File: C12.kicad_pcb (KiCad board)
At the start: 4 copper layers, 90.3 x 26.6 mm, 85 parts, among them IC1 BD63573NUV-E2, IC3 74HC595BQ,115, J1 Conn_01x06, J2 Slot Connector, J3 Conn_01x06, U1 74AHC1G08, U15 MCP9700AT-ETT, U3 INA181, U4 LM393, U5 MIC5235-3.3, U6 AVR64DA48, U8 OPA521, X1 ASE-24MHz

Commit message: Initial commit
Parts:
- IC3: footprint _Samac:74HC595BQ115 -> RTB:74HC595BQ115
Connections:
- net /RailcomRX/RX+ renamed /Railcom/RX+
- net /RailcomRX/RX- renamed /Railcom/RX-
- IC1 pad 11: GNDD -> (no net)

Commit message: Initial commit
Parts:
- moved HS1 15.0 mm to (130.9, 32.5)

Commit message: initial
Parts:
- added Q1: BC847BDW1, Package_TO_SOT_SMD:SOT-363_SC-70-6, F.Cu at (140.1, 45.7)
- added R10: 68k, Resistor_SMD:R_0603_1608Metric, F.Cu at (117.8, 42.5)
- added R11: 33k, Resistor_SMD:R_0603_1608Metric, F.Cu at (119.2, 42.5)
- added R12: 10k, Resistor_SMD:R_0603_1608Metric, F.Cu at (92.7, 42.4)
- added R18: 220k, Resistor_SMD:R_0603_1608Metric, F.Cu at (115.6, 29.4)
- added R2: 100k, Resistor_SMD:R_0603_1608Metric, F.Cu at (116.3, 42.5)
- added R21: 9.1k, Resistor_SMD:R_0603_1608Metric, F.Cu at (115.6, 27.9)
- added R26: 160, Inductor_SMD:L_1206_3216Metric, F.Cu at (136.1, 44.8)
- added R32: 160, Inductor_SMD:L_1206_3216Metric, F.Cu at (136.1, 47.2)
- added R33: 1k, Inductor_SMD:L_0603_1608Metric, F.Cu at (136.9, 42.9)
- added R34: 1k, Inductor_SMD:L_0603_1608Metric, F.Cu at (137.0, 41.4)
- R36: value 10k -> 22k
- moved HS1 15.3 mm to (133.7, 17.5)
- moved R36 6.90 mm to (120.7, 42.5), turned to 90 degrees
- moved R35 4.17 mm to (141.0, 42.8)
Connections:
- IC1 pad 11: (no net) -> GNDD
- J2 pad 17: (no net) -> GNDD
- J2 pad 18: (no net) -> GNDD
- J2 pad 24: (no net) -> iCONFIG
- R36 pad 2: GNDD -> iLIM3
- U6 pad 16: (no net) -> iLIM0
- U6 pad 17: (no net) -> iLIM1
- U6 pad 18: (no net) -> iLIM2
- U6 pad 19: (no net) -> iLIM3
- U6 pad 20: (no net) -> iCONFIG
- U6 pad 22: (no net) -> iSENSE
- U6 pad 23: (no net) -> TRKgnd
- U6 pad 30: (no net) -> rSENSE
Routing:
- net TRKgnd: track 0.00 -> 53.6 mm
- net rSENSE: track 0.00 -> 50.3 mm, vias 0 -> 2
- net iLIM3: track 0.00 -> 38.2 mm
- net iLIM2: track 0.00 -> 36.4 mm
- net iLIM1: track 0.00 -> 34.8 mm
- net iLIM0: track 0.00 -> 33.2 mm
- net iCONFIG: track 0.00 -> 14.2 mm, vias 0 -> 2
- net Net-(R10-Pad1): track 6.26 -> 18.5 mm, vias 0 -> 2
- net Net-(Q1-Pad5): track 0.00 -> 7.06 mm
- net DCC-A': track 37.4 -> 44.3 mm, vias 2 -> 3
- net Net-(Q1-Pad2): track 0.00 -> 5.15 mm
- net iSENSE: track 59.6 -> 64.4 mm, vias 2 -> 3
- net V24.rx: track 16.7 -> 21.4 mm
- net ~V24.rts: track 22.4 -> 27.1 mm, vias 2 -> 0
- net GNDD: track 92.4 -> 87.7 mm, vias 51 -> 59
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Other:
- rule via_min_size: 0.6 -> 0.5
- board text added: "Debug"
- board text added: "fschum '24"
- board text removed: "F.Schumacher'22"

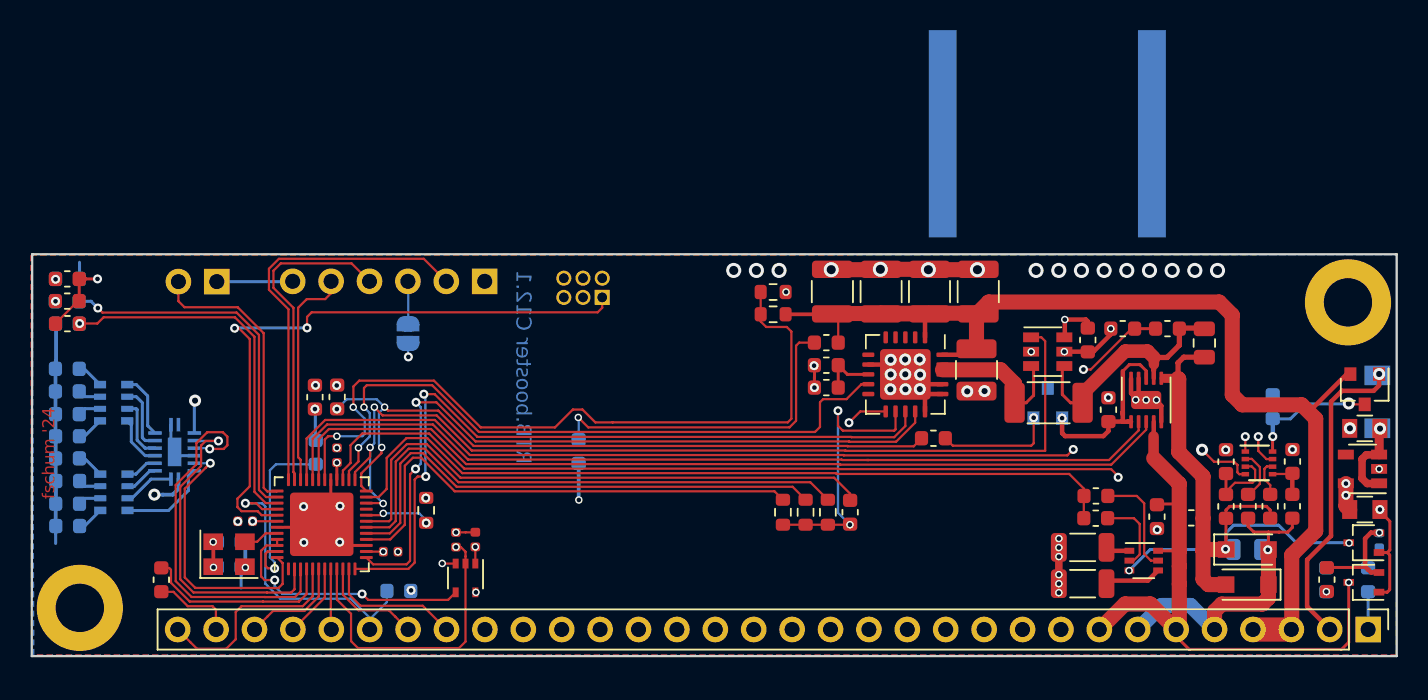
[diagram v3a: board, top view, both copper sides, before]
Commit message: mod: optimized for PCB assembly
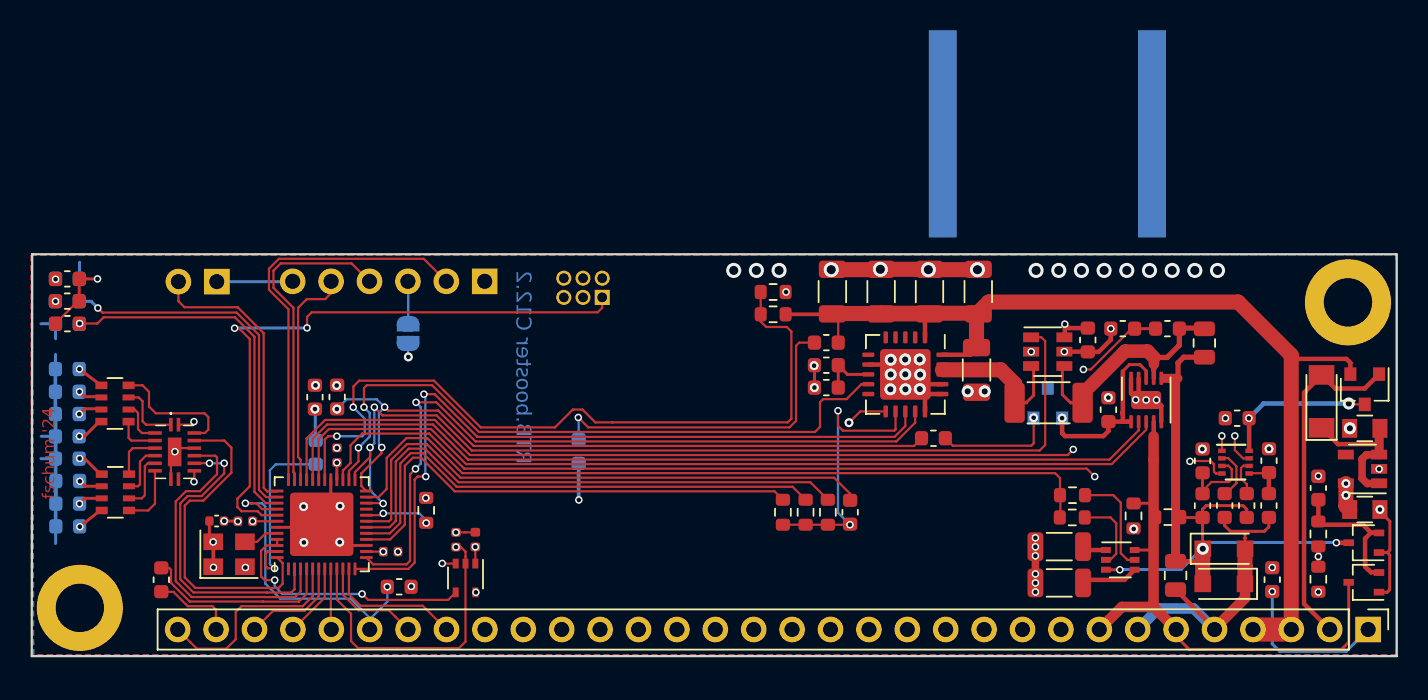
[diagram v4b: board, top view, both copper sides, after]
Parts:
- removed C7: 2.2u, Capacitor_SMD:C_0603_1608Metric
- C1: value 4.7uF -> 10uF; footprint Capacitor_SMD:C_1210_3225Metric -> Capacitor_SMD:C_1206_3216Metric
- C10, C14, C15, C20: value 100n -> 100nF
- C11: footprint Capacitor_SMD:C_0402_1005Metric -> Capacitor_SMD:C_0603_1608Metric; moved to F.Cu
- C19, C4, C8, C9: value 47uF -> 10uF; footprint Capacitor_SMD:C_1210_3225Metric -> Capacitor_SMD:C_1206_3216Metric
- C2: value 10uF/16V -> 10uF
- C3: value 2.2uF/10V -> 10uF
- C5: value 1u -> 1uF; moved to F.Cu
- C6: value 100n -> 100nF; footprint Capacitor_SMD:C_0603_1608Metric -> Capacitor_SMD:C_0402_1005Metric; moved to F.Cu
- D17, IC3, R14, R22, R29, R9: moved to F.Cu
- Q1: value BC847BDW1 -> BC847BDW1T1G
- R10: value 68k -> 56k
- R24: value 2.2k -> 3.3k
- R25: value 47k -> 3.3k
- R26, R32: value 160 -> 300
- R28, R39: value 100k -> 3.3k
- R30: value 6.8k -> 3.3k
- R33, R34, R35, R46: footprint Inductor_SMD:L_0603_1608Metric -> Resistor_SMD:R_0603_1608Metric
- R7, R8: value 80k -> 82k
- RN3, RN4: value 3.3k -> 4.7k; moved to F.Cu
- U3: value INA181 -> INA181A1
- U4: footprint _Local:DFN-8-1EP_NG_2x2mm_Pitch0.5mm -> RTB:DFN-8-1EP_NG_2x2mm_Pitch0.5mm
- moved D14 10.4 mm to (69.0, 43.4)
- moved D38 10.4 mm to (68.9, 33.0)
- moved D32 7.42 mm to (69.0, 41.9)
- moved D37 7.40 mm to (68.9, 34.5)
- moved R22 6.34 mm to (148.6, 47.0)
- moved RN4 5.93 mm to (72.1, 41.2)
- moved RN3 5.87 mm to (72.1, 35.3)
- moved C11 5.31 mm to (151.7, 40.9), turned to 90 degrees
- moved R9 5.05 mm to (142.2, 46.7), turned to 90 degrees
- moved D36 4.43 mm to (68.9, 36.0)
- moved D33 4.42 mm to (69.0, 40.4)
- moved D17 3.69 mm to (151.9, 35.2)
- moved R13 3.07 mm to (151.7, 43.9)
- moved C5 2.47 mm to (146.3, 36.3), turned to 0 degrees
- moved C6 1.61 mm to (78.8, 43.1)
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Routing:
- net Net-(J2-Pad1): track 2.50 -> 10.6 mm, vias 0 -> 1
- net Net-(C2-Pad1): track 7.00 -> 11.2 mm, vias 1 -> 0
- net MOSI0: track 18.1 -> 21.8 mm, vias 1 -> 0
- net SS0: track 25.4 -> 21.8 mm, vias 1 -> 0
- net VTRACK: track 6.66 -> 9.48 mm, vias 1 -> 0
- net Net-(IC3-Pad15): track 6.09 -> 8.56 mm
- net DCC-B: track 40.4 -> 38.1 mm, vias 1 -> 0
- net VREG: track 75.8 -> 73.6 mm
- net 3.3V: track 37.9 -> 36.0 mm
- net Vrail: track 20.8 -> 22.6 mm, vias 1 -> 0
- net Vrcm: track 8.66 -> 10.3 mm
- net Net-(R19-Pad2): track 61.5 -> 60.0 mm
- net RCM.pol: track 79.5 -> 78.0 mm
- net GNDD: track 87.7 -> 86.2 mm, vias 59 -> 65
- net DCC-A: track 20.4 -> 21.8 mm, vias 1 -> 0
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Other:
- rule pad_to_mask_clearance: 0.2 -> 0
- board text added: "RTB.booster C12.2"
- board text removed: "RTB.booster C12.1"

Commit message: mod: optimized for PCB assembly
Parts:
- C1, C19, C4, C8, C9: value 10uF -> 22uF
- J1: value Conn_01x06 -> Debug IF
- J3: value Conn_01x06 -> UPDI
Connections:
- net VTRACK renamed Net-(C11-Pad1)

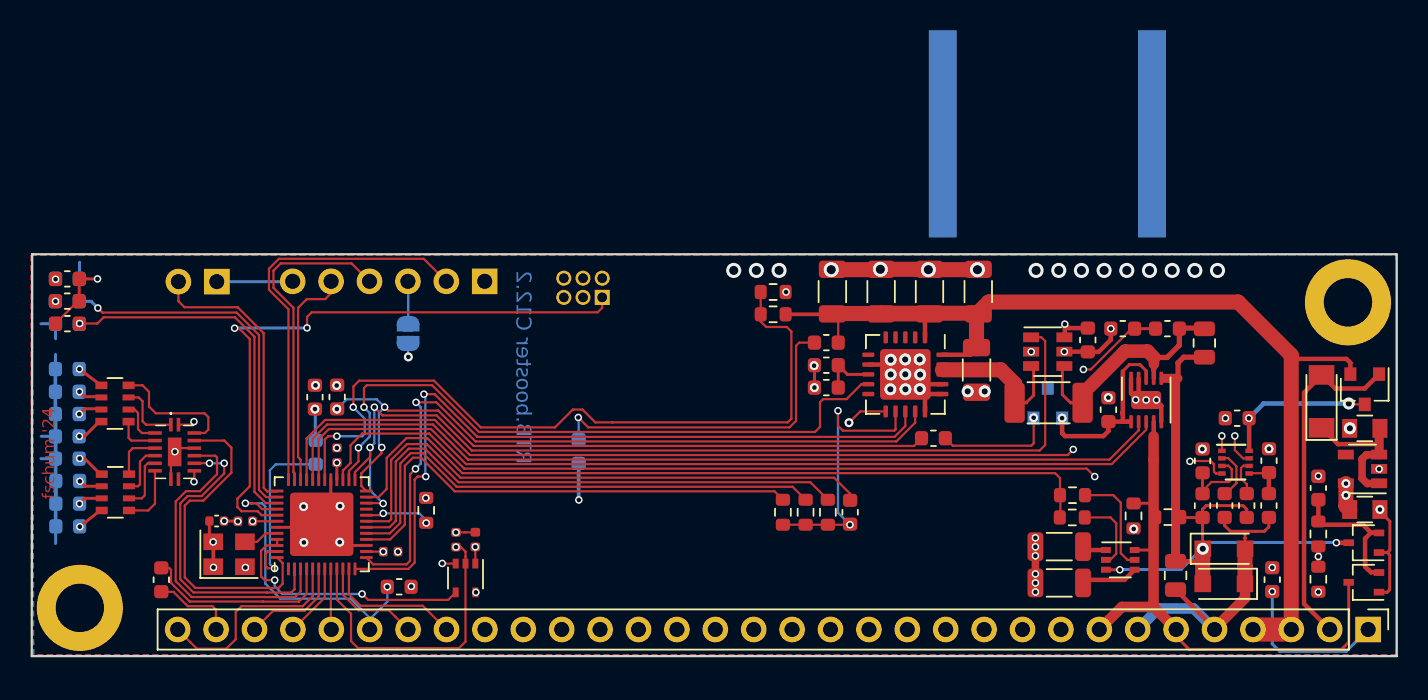
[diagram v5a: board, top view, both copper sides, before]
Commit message: upgrade to Kicad 9
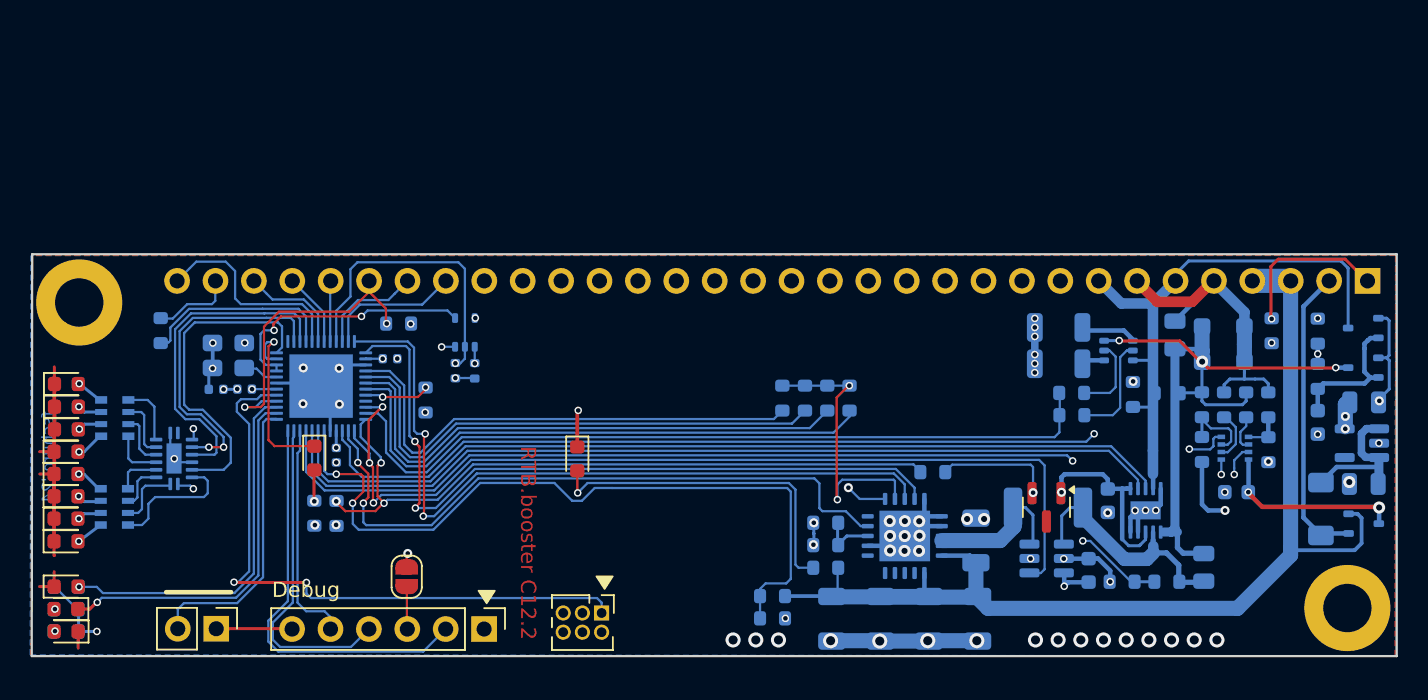
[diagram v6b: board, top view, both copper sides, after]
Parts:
- removed HS1: Heatsink, Heatsink:Heatsink_AAVID_573300D00010G_TO-263
- C1, C10, C11, C14, C15, C19, C20, C21, C4, C5, C6, C8, C9, D17, D3, D4, D6, D9, H1, H3, IC1, J2, R1, R10, R11, R12, R13, R14, R18, R19, R2, R20, R21, R22, R23, R24, R25, R26, R27, R28, R29, R3, R30, R31, R32, R33, R34, R35, R36, R37, R38, R39, R4, R46, R5, R6, R7, R8, R9, RN3, RN4, U1, U3, U4, U6, U8, X1: moved to B.Cu
- C2, C3: footprint Capacitors_SMD:C_0805 -> Capacitor_SMD:C_0805_2012Metric; moved to B.Cu
- D12, D13, D14, D16, D32, D33, D34, D35, D36, D37, D5, D8, J1, J3, JP1, JP2, U15: moved to F.Cu
- D31: footprint Package_TO_SOT_SMD:SOT-23 -> Package_TO_SOT_SMD:SOT-323_SC-70; moved to B.Cu
- D38: value LED_Small -> LED(wht); moved to F.Cu
- IC3: footprint RTB:74HC595BQ115 -> Package_DFN_QFN:DHVQFN-16-1EP_2.5x3.5mm_P0.5mm_EP1x2mm; moved to B.Cu
- Q1: value BC847BDW1T1G -> BC847BDW1; moved to B.Cu
- R15, R16: value 10k -> n.f.; moved to B.Cu
- R17: value 0.05 -> 0.025; moved to B.Cu
- U5: footprint TO_SOT_Packages_SMD:SOT-23-5 -> Package_TO_SOT_SMD:SOT-23-5; moved to B.Cu
- moved D16 23.3 mm to (68.8, 50.4)
- moved R28 23.3 mm to (68.8, 50.4)
- moved J2 23.1 mm to (154.9, 27.2), turned to 90 degrees
- moved J1 23.0 mm to (96.5, 50.2), turned to -90 degrees
- moved JP1 23.0 mm to (78.8, 50.2), turned to -90 degrees
- moved C19 21.6 mm to (122.7, 49.5), turned to -90 degrees
- moved C4 21.6 mm to (125.9, 49.5), turned to -90 degrees
- moved C8 21.6 mm to (129.1, 49.5), turned to -90 degrees
- moved C9 21.6 mm to (119.5, 49.5), turned to -90 degrees
- moved R21 21.6 mm to (115.6, 49.5)
- moved J3 20.9 mm to (104.3, 49.2), turned to -90 degrees
- moved R24 20.4 mm to (68.8, 48.9)
- moved D13 20.4 mm to (68.8, 48.9)
- moved H3 20.2 mm to (153.6, 48.8)
- moved H1 20.2 mm to (69.7, 28.6)
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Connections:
- net ~BUS.bsi renamed ~{BUS.bsi}
- net ~BUS.bso renamed ~{BUS.bso}
- net ~BUS.rts renamed ~{BUS.rts}
- net ~RESET renamed ~{RESET}
- net ~V24.cts renamed ~{V24.cts}
- net ~V24.rts renamed ~{V24.rts}
- IC3 pad 9: (no net) -> unconnected-(IC3-Q7S-Pad9)
- J2 pad 10: (no net) -> unconnected-(J2-Pin_10-Pad10)
- J2 pad 11: (no net) -> unconnected-(J2-Pin_11-Pad11)
- J2 pad 12: (no net) -> unconnected-(J2-Pin_12-Pad12)
- J2 pad 13: (no net) -> unconnected-(J2-Pin_13-Pad13)
- J2 pad 14: (no net) -> unconnected-(J2-Pin_14-Pad14)
- J2 pad 19: (no net) -> unconnected-(J2-Pin_19-Pad19)
- J2 pad 20: (no net) -> unconnected-(J2-Pin_20-Pad20)
- J2 pad 21: (no net) -> unconnected-(J2-Pin_21-Pad21)
- J2 pad 22: (no net) -> unconnected-(J2-Pin_22-Pad22)
- J2 pad 23: (no net) -> unconnected-(J2-Pin_23-Pad23)
- J2 pad 9: (no net) -> unconnected-(J2-Pin_9-Pad9)
- J3 pad 3: (no net) -> unconnected-(J3-Pin_3-Pad3)
- J3 pad 4: (no net) -> unconnected-(J3-Pin_4-Pad4)
- J3 pad 5: (no net) -> unconnected-(J3-Pin_5-Pad5)
- U5 pad 4: (no net) -> unconnected-(U5-BP-Pad4)
- U6 pad 1: (no net) -> unconnected-(U6-PA5-Pad1)
- U6 pad 21: (no net) -> unconnected-(U6-PD1-Pad21)
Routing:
- net 3.3V: track 36.0 -> 40.3 mm
- net VREG: track 73.6 -> 76.5 mm
- net Vrail: track 22.6 -> 19.9 mm
- net Vrcm: track 10.3 -> 12.3 mm
- added copper zone on In2.Cu, net 3.3V
- added copper zone on In1.Cu, net GNDD
- removed copper zone on VDD.Cu, net 3.3V
- removed copper zone on GND.Cu, net GNDD
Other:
- net class Default removed
- net class Power removed
